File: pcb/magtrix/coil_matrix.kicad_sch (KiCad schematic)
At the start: 200 parts

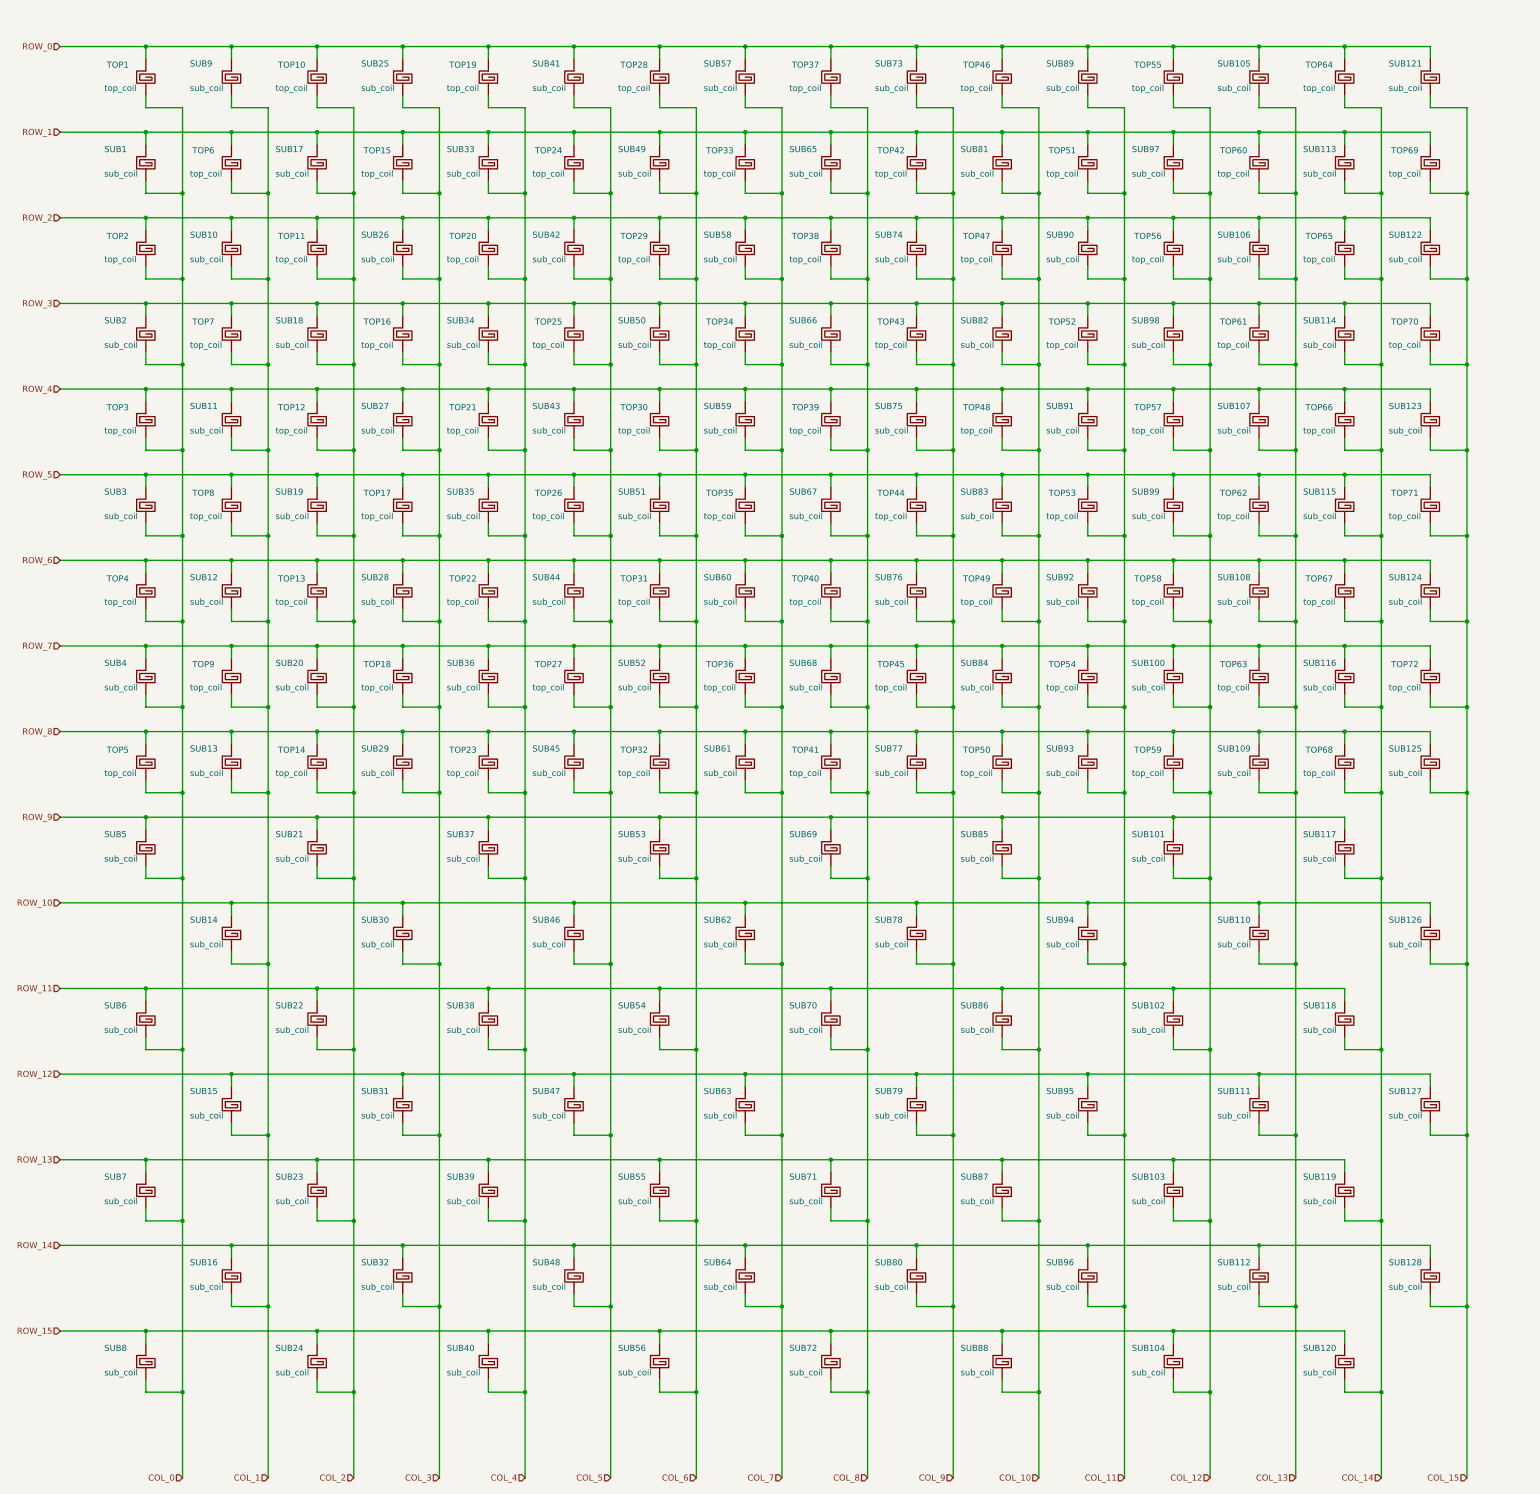
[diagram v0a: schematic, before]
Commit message: Finished schematics and footprints, need to redo the placement
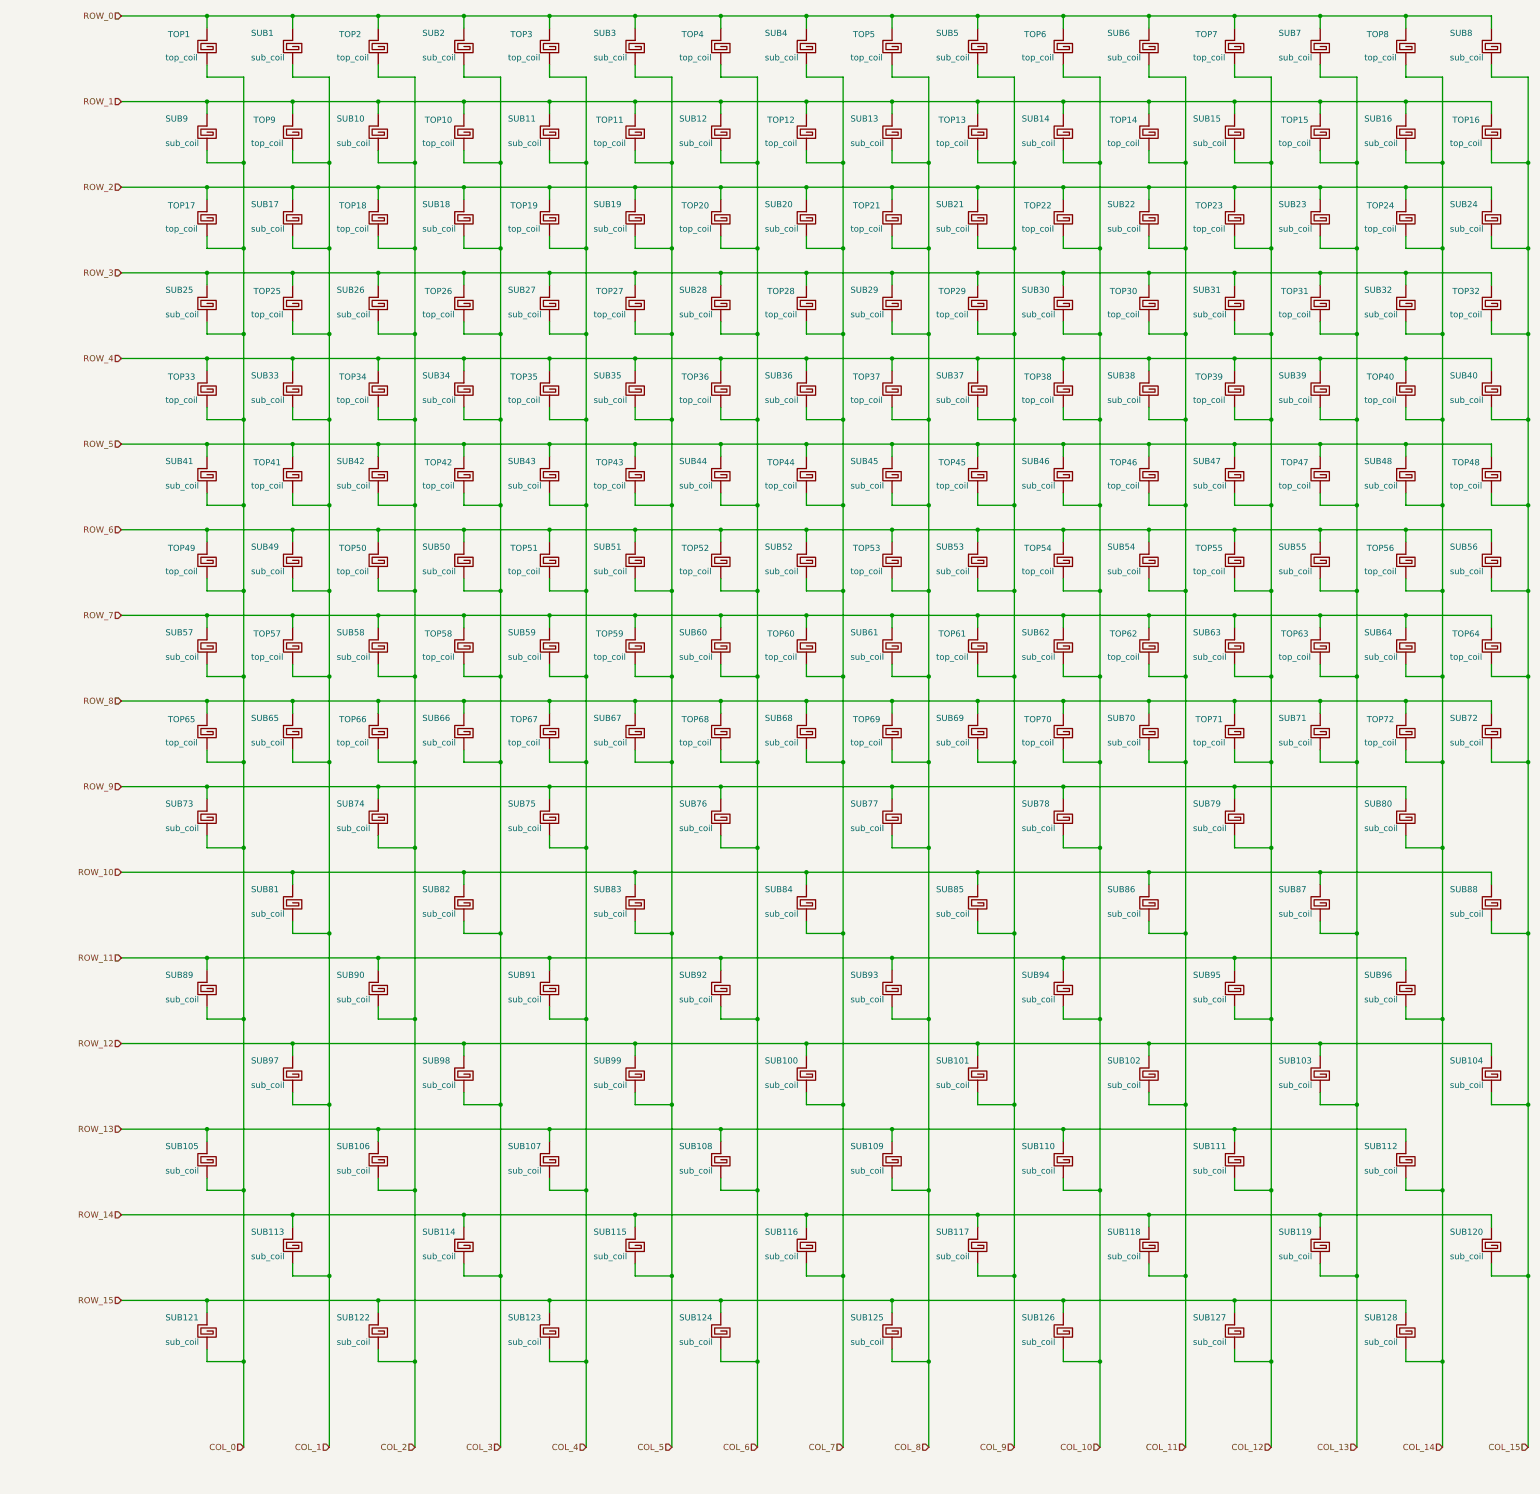
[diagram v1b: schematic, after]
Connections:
- net COL_0: now also SUB105.2 (B), SUB121.2 (B), SUB25.2 (B), SUB41.2 (B), SUB57.2 (B), SUB73.2 (B), SUB89.2 (B), SUB9.2 (B), TOP17.2 (B), TOP33.2 (B), TOP49.2 (B), TOP65.2 (B); no longer SUB1.2 (B), SUB2.2 (B), SUB3.2 (B), SUB4.2 (B), SUB5.2 (B), SUB6.2 (B), SUB7.2 (B), SUB8.2 (B), TOP2.2 (B), TOP3.2 (B), TOP4.2 (B), TOP5.2 (B)
- net COL_1: now also SUB1.2 (B), SUB113.2 (B), SUB17.2 (B), SUB33.2 (B), SUB49.2 (B), SUB65.2 (B), SUB81.2 (B), SUB97.2 (B), TOP25.2 (B), TOP41.2 (B), TOP57.2 (B); no longer SUB10.2 (B), SUB11.2 (B), SUB12.2 (B), SUB13.2 (B), SUB14.2 (B), SUB15.2 (B), SUB16.2 (B), SUB9.2 (B), TOP6.2 (B), TOP7.2 (B), TOP8.2 (B)
- net COL_10: now also SUB110.2 (B), SUB126.2 (B), SUB14.2 (B), SUB30.2 (B), SUB46.2 (B), SUB62.2 (B), SUB78.2 (B), SUB94.2 (B), TOP22.2 (B), TOP38.2 (B), TOP54.2 (B), TOP6.2 (B), TOP70.2 (B); no longer SUB81.2 (B), SUB82.2 (B), SUB83.2 (B), SUB84.2 (B), SUB85.2 (B), SUB86.2 (B), SUB87.2 (B), SUB88.2 (B), TOP46.2 (B), TOP47.2 (B), TOP48.2 (B), TOP49.2 (B), TOP50.2 (B)
- net COL_11: now also SUB102.2 (B), SUB118.2 (B), SUB22.2 (B), SUB38.2 (B), SUB54.2 (B), SUB6.2 (B), SUB70.2 (B), SUB86.2 (B), TOP14.2 (B), TOP30.2 (B), TOP46.2 (B), TOP62.2 (B); no longer SUB89.2 (B), SUB90.2 (B), SUB91.2 (B), SUB92.2 (B), SUB93.2 (B), SUB94.2 (B), SUB95.2 (B), SUB96.2 (B), TOP51.2 (B), TOP52.2 (B), TOP53.2 (B), TOP54.2 (B)
- net COL_12: now also SUB111.2 (B), SUB127.2 (B), SUB15.2 (B), SUB31.2 (B), SUB47.2 (B), SUB63.2 (B), SUB79.2 (B), SUB95.2 (B), TOP23.2 (B), TOP39.2 (B), TOP7.2 (B), TOP71.2 (B); no longer SUB100.2 (B), SUB101.2 (B), SUB102.2 (B), SUB103.2 (B), SUB104.2 (B), SUB97.2 (B), SUB98.2 (B), SUB99.2 (B), TOP56.2 (B), TOP57.2 (B), TOP58.2 (B), TOP59.2 (B)
- net COL_13: now also SUB103.2 (B), SUB119.2 (B), SUB23.2 (B), SUB39.2 (B), SUB55.2 (B), SUB7.2 (B), SUB71.2 (B), SUB87.2 (B), TOP15.2 (B), TOP31.2 (B), TOP47.2 (B); no longer SUB105.2 (B), SUB106.2 (B), SUB107.2 (B), SUB108.2 (B), SUB109.2 (B), SUB110.2 (B), SUB111.2 (B), SUB112.2 (B), TOP60.2 (B), TOP61.2 (B), TOP62.2 (B)
- net COL_14: now also SUB112.2 (B), SUB128.2 (B), SUB16.2 (B), SUB32.2 (B), SUB48.2 (B), SUB64.2 (B), SUB80.2 (B), SUB96.2 (B), TOP24.2 (B), TOP40.2 (B), TOP56.2 (B), TOP72.2 (B), TOP8.2 (B); no longer SUB113.2 (B), SUB114.2 (B), SUB115.2 (B), SUB116.2 (B), SUB117.2 (B), SUB118.2 (B), SUB119.2 (B), SUB120.2 (B), TOP64.2 (B), TOP65.2 (B), TOP66.2 (B), TOP67.2 (B), TOP68.2 (B)
- net COL_15: now also SUB104.2 (B), SUB120.2 (B), SUB24.2 (B), SUB40.2 (B), SUB56.2 (B), SUB72.2 (B), SUB8.2 (B), SUB88.2 (B), TOP16.2 (B), TOP32.2 (B), TOP48.2 (B), TOP64.2 (B); no longer SUB121.2 (B), SUB122.2 (B), SUB123.2 (B), SUB124.2 (B), SUB125.2 (B), SUB126.2 (B), SUB127.2 (B), SUB128.2 (B), TOP69.2 (B), TOP70.2 (B), TOP71.2 (B), TOP72.2 (B)
- net COL_2: now also SUB10.2 (B), SUB106.2 (B), SUB122.2 (B), SUB26.2 (B), SUB42.2 (B), SUB58.2 (B), SUB74.2 (B), SUB90.2 (B), TOP18.2 (B), TOP2.2 (B), TOP34.2 (B), TOP50.2 (B), TOP66.2 (B); no longer SUB17.2 (B), SUB18.2 (B), SUB19.2 (B), SUB20.2 (B), SUB21.2 (B), SUB22.2 (B), SUB23.2 (B), SUB24.2 (B), TOP10.2 (B), TOP11.2 (B), TOP12.2 (B), TOP13.2 (B), TOP14.2 (B)
- net COL_3: now also SUB114.2 (B), SUB18.2 (B), SUB2.2 (B), SUB34.2 (B), SUB50.2 (B), SUB66.2 (B), SUB82.2 (B), SUB98.2 (B), TOP10.2 (B), TOP26.2 (B), TOP42.2 (B), TOP58.2 (B); no longer SUB25.2 (B), SUB26.2 (B), SUB27.2 (B), SUB28.2 (B), SUB29.2 (B), SUB30.2 (B), SUB31.2 (B), SUB32.2 (B), TOP15.2 (B), TOP16.2 (B), TOP17.2 (B), TOP18.2 (B)
- net COL_4: now also SUB107.2 (B), SUB11.2 (B), SUB123.2 (B), SUB27.2 (B), SUB43.2 (B), SUB59.2 (B), SUB75.2 (B), SUB91.2 (B), TOP3.2 (B), TOP35.2 (B), TOP51.2 (B), TOP67.2 (B); no longer SUB33.2 (B), SUB34.2 (B), SUB35.2 (B), SUB36.2 (B), SUB37.2 (B), SUB38.2 (B), SUB39.2 (B), SUB40.2 (B), TOP20.2 (B), TOP21.2 (B), TOP22.2 (B), TOP23.2 (B)
- net COL_5: now also SUB115.2 (B), SUB19.2 (B), SUB3.2 (B), SUB35.2 (B), SUB51.2 (B), SUB67.2 (B), SUB83.2 (B), SUB99.2 (B), TOP11.2 (B), TOP43.2 (B), TOP59.2 (B); no longer SUB41.2 (B), SUB42.2 (B), SUB43.2 (B), SUB44.2 (B), SUB45.2 (B), SUB46.2 (B), SUB47.2 (B), SUB48.2 (B), TOP24.2 (B), TOP25.2 (B), TOP26.2 (B)
- net COL_6: now also SUB108.2 (B), SUB12.2 (B), SUB124.2 (B), SUB28.2 (B), SUB44.2 (B), SUB60.2 (B), SUB76.2 (B), SUB92.2 (B), TOP20.2 (B), TOP36.2 (B), TOP4.2 (B), TOP52.2 (B), TOP68.2 (B); no longer SUB49.2 (B), SUB50.2 (B), SUB51.2 (B), SUB52.2 (B), SUB53.2 (B), SUB54.2 (B), SUB55.2 (B), SUB56.2 (B), TOP28.2 (B), TOP29.2 (B), TOP30.2 (B), TOP31.2 (B), TOP32.2 (B)
- net COL_7: now also SUB100.2 (B), SUB116.2 (B), SUB20.2 (B), SUB36.2 (B), SUB4.2 (B), SUB52.2 (B), SUB68.2 (B), SUB84.2 (B), TOP12.2 (B), TOP28.2 (B), TOP44.2 (B), TOP60.2 (B); no longer SUB57.2 (B), SUB58.2 (B), SUB59.2 (B), SUB60.2 (B), SUB61.2 (B), SUB62.2 (B), SUB63.2 (B), SUB64.2 (B), TOP33.2 (B), TOP34.2 (B), TOP35.2 (B), TOP36.2 (B)
- net COL_8: now also SUB109.2 (B), SUB125.2 (B), SUB13.2 (B), SUB29.2 (B), SUB45.2 (B), SUB61.2 (B), SUB77.2 (B), SUB93.2 (B), TOP21.2 (B), TOP5.2 (B), TOP53.2 (B), TOP69.2 (B); no longer SUB65.2 (B), SUB66.2 (B), SUB67.2 (B), SUB68.2 (B), SUB69.2 (B), SUB70.2 (B), SUB71.2 (B), SUB72.2 (B), TOP38.2 (B), TOP39.2 (B), TOP40.2 (B), TOP41.2 (B)
- net COL_9: now also SUB101.2 (B), SUB117.2 (B), SUB21.2 (B), SUB37.2 (B), SUB5.2 (B), SUB53.2 (B), SUB69.2 (B), SUB85.2 (B), TOP13.2 (B), TOP29.2 (B), TOP61.2 (B); no longer SUB73.2 (B), SUB74.2 (B), SUB75.2 (B), SUB76.2 (B), SUB77.2 (B), SUB78.2 (B), SUB79.2 (B), SUB80.2 (B), TOP42.2 (B), TOP43.2 (B), TOP44.2 (B)
- net ROW_0: now also SUB1.1 (A), SUB2.1 (A), SUB3.1 (A), SUB4.1 (A), SUB5.1 (A), SUB6.1 (A), SUB7.1 (A), SUB8.1 (A), TOP2.1 (A), TOP3.1 (A), TOP4.1 (A), TOP5.1 (A), TOP6.1 (A), TOP7.1 (A), TOP8.1 (A); no longer SUB105.1 (A), SUB121.1 (A), SUB25.1 (A), SUB41.1 (A), SUB57.1 (A), SUB73.1 (A), SUB89.1 (A), SUB9.1 (A), TOP10.1 (A), TOP19.1 (A), TOP28.1 (A), TOP37.1 (A), TOP46.1 (A), TOP55.1 (A), TOP64.1 (A)
- net ROW_1: now also SUB10.1 (A), SUB11.1 (A), SUB12.1 (A), SUB13.1 (A), SUB14.1 (A), SUB15.1 (A), SUB16.1 (A), SUB9.1 (A), TOP10.1 (A), TOP11.1 (A), TOP12.1 (A), TOP13.1 (A), TOP14.1 (A), TOP16.1 (A), TOP9.1 (A); no longer SUB1.1 (A), SUB113.1 (A), SUB17.1 (A), SUB33.1 (A), SUB49.1 (A), SUB65.1 (A), SUB81.1 (A), SUB97.1 (A), TOP24.1 (A), TOP33.1 (A), TOP42.1 (A), TOP51.1 (A), TOP6.1 (A), TOP60.1 (A), TOP69.1 (A)
- net ROW_10: now also SUB81.1 (A), SUB82.1 (A), SUB83.1 (A), SUB84.1 (A), SUB85.1 (A), SUB86.1 (A), SUB87.1 (A), SUB88.1 (A); no longer SUB110.1 (A), SUB126.1 (A), SUB14.1 (A), SUB30.1 (A), SUB46.1 (A), SUB62.1 (A), SUB78.1 (A), SUB94.1 (A)
- net ROW_11: now also SUB89.1 (A), SUB90.1 (A), SUB91.1 (A), SUB92.1 (A), SUB93.1 (A), SUB94.1 (A), SUB95.1 (A), SUB96.1 (A); no longer SUB102.1 (A), SUB118.1 (A), SUB22.1 (A), SUB38.1 (A), SUB54.1 (A), SUB6.1 (A), SUB70.1 (A), SUB86.1 (A)
- net ROW_12: now also SUB100.1 (A), SUB101.1 (A), SUB102.1 (A), SUB103.1 (A), SUB104.1 (A), SUB97.1 (A), SUB98.1 (A), SUB99.1 (A); no longer SUB111.1 (A), SUB127.1 (A), SUB15.1 (A), SUB31.1 (A), SUB47.1 (A), SUB63.1 (A), SUB79.1 (A), SUB95.1 (A)
- net ROW_13: now also SUB105.1 (A), SUB106.1 (A), SUB107.1 (A), SUB108.1 (A), SUB109.1 (A), SUB110.1 (A), SUB111.1 (A), SUB112.1 (A); no longer SUB103.1 (A), SUB119.1 (A), SUB23.1 (A), SUB39.1 (A), SUB55.1 (A), SUB7.1 (A), SUB71.1 (A), SUB87.1 (A)
- net ROW_14: now also SUB113.1 (A), SUB114.1 (A), SUB115.1 (A), SUB116.1 (A), SUB117.1 (A), SUB118.1 (A), SUB119.1 (A), SUB120.1 (A); no longer SUB112.1 (A), SUB128.1 (A), SUB16.1 (A), SUB32.1 (A), SUB48.1 (A), SUB64.1 (A), SUB80.1 (A), SUB96.1 (A)
- net ROW_15: now also SUB121.1 (A), SUB122.1 (A), SUB123.1 (A), SUB124.1 (A), SUB125.1 (A), SUB126.1 (A), SUB127.1 (A), SUB128.1 (A); no longer SUB104.1 (A), SUB120.1 (A), SUB24.1 (A), SUB40.1 (A), SUB56.1 (A), SUB72.1 (A), SUB8.1 (A), SUB88.1 (A)
- net ROW_2: now also SUB17.1 (A), SUB18.1 (A), SUB19.1 (A), SUB20.1 (A), SUB21.1 (A), SUB22.1 (A), SUB23.1 (A), SUB24.1 (A), TOP17.1 (A), TOP18.1 (A), TOP19.1 (A), TOP21.1 (A), TOP22.1 (A), TOP23.1 (A), TOP24.1 (A); no longer SUB10.1 (A), SUB106.1 (A), SUB122.1 (A), SUB26.1 (A), SUB42.1 (A), SUB58.1 (A), SUB74.1 (A), SUB90.1 (A), TOP11.1 (A), TOP2.1 (A), TOP29.1 (A), TOP38.1 (A), TOP47.1 (A), TOP56.1 (A), TOP65.1 (A)
- net ROW_3: now also SUB25.1 (A), SUB26.1 (A), SUB27.1 (A), SUB28.1 (A), SUB29.1 (A), SUB30.1 (A), SUB31.1 (A), SUB32.1 (A), TOP26.1 (A), TOP27.1 (A), TOP28.1 (A), TOP29.1 (A), TOP30.1 (A), TOP31.1 (A), TOP32.1 (A); no longer SUB114.1 (A), SUB18.1 (A), SUB2.1 (A), SUB34.1 (A), SUB50.1 (A), SUB66.1 (A), SUB82.1 (A), SUB98.1 (A), TOP16.1 (A), TOP34.1 (A), TOP43.1 (A), TOP52.1 (A), TOP61.1 (A), TOP7.1 (A), TOP70.1 (A)
- net ROW_4: now also SUB33.1 (A), SUB34.1 (A), SUB35.1 (A), SUB36.1 (A), SUB37.1 (A), SUB38.1 (A), SUB39.1 (A), SUB40.1 (A), TOP33.1 (A), TOP34.1 (A), TOP35.1 (A), TOP36.1 (A), TOP37.1 (A), TOP38.1 (A), TOP40.1 (A); no longer SUB107.1 (A), SUB11.1 (A), SUB123.1 (A), SUB27.1 (A), SUB43.1 (A), SUB59.1 (A), SUB75.1 (A), SUB91.1 (A), TOP12.1 (A), TOP21.1 (A), TOP3.1 (A), TOP30.1 (A), TOP48.1 (A), TOP57.1 (A), TOP66.1 (A)
- net ROW_5: now also SUB41.1 (A), SUB42.1 (A), SUB43.1 (A), SUB44.1 (A), SUB45.1 (A), SUB46.1 (A), SUB47.1 (A), SUB48.1 (A), TOP41.1 (A), TOP42.1 (A), TOP43.1 (A), TOP45.1 (A), TOP46.1 (A), TOP47.1 (A), TOP48.1 (A); no longer SUB115.1 (A), SUB19.1 (A), SUB3.1 (A), SUB35.1 (A), SUB51.1 (A), SUB67.1 (A), SUB83.1 (A), SUB99.1 (A), TOP17.1 (A), TOP26.1 (A), TOP35.1 (A), TOP53.1 (A), TOP62.1 (A), TOP71.1 (A), TOP8.1 (A)
- net ROW_6: now also SUB49.1 (A), SUB50.1 (A), SUB51.1 (A), SUB52.1 (A), SUB53.1 (A), SUB54.1 (A), SUB55.1 (A), SUB56.1 (A), TOP50.1 (A), TOP51.1 (A), TOP52.1 (A), TOP53.1 (A), TOP54.1 (A), TOP55.1 (A), TOP56.1 (A); no longer SUB108.1 (A), SUB12.1 (A), SUB124.1 (A), SUB28.1 (A), SUB44.1 (A), SUB60.1 (A), SUB76.1 (A), SUB92.1 (A), TOP13.1 (A), TOP22.1 (A), TOP31.1 (A), TOP4.1 (A), TOP40.1 (A), TOP58.1 (A), TOP67.1 (A)
- net ROW_7: now also SUB57.1 (A), SUB58.1 (A), SUB59.1 (A), SUB60.1 (A), SUB61.1 (A), SUB62.1 (A), SUB63.1 (A), SUB64.1 (A), TOP57.1 (A), TOP58.1 (A), TOP59.1 (A), TOP60.1 (A), TOP61.1 (A), TOP62.1 (A), TOP64.1 (A); no longer SUB100.1 (A), SUB116.1 (A), SUB20.1 (A), SUB36.1 (A), SUB4.1 (A), SUB52.1 (A), SUB68.1 (A), SUB84.1 (A), TOP18.1 (A), TOP27.1 (A), TOP36.1 (A), TOP45.1 (A), TOP54.1 (A), TOP72.1 (A), TOP9.1 (A)
- net ROW_8: now also SUB65.1 (A), SUB66.1 (A), SUB67.1 (A), SUB68.1 (A), SUB69.1 (A), SUB70.1 (A), SUB71.1 (A), SUB72.1 (A), TOP65.1 (A), TOP66.1 (A), TOP67.1 (A), TOP69.1 (A), TOP70.1 (A), TOP71.1 (A), TOP72.1 (A); no longer SUB109.1 (A), SUB125.1 (A), SUB13.1 (A), SUB29.1 (A), SUB45.1 (A), SUB61.1 (A), SUB77.1 (A), SUB93.1 (A), TOP14.1 (A), TOP23.1 (A), TOP32.1 (A), TOP41.1 (A), TOP5.1 (A), TOP50.1 (A), TOP59.1 (A)
- net ROW_9: now also SUB73.1 (A), SUB74.1 (A), SUB75.1 (A), SUB76.1 (A), SUB77.1 (A), SUB78.1 (A), SUB79.1 (A), SUB80.1 (A); no longer SUB101.1 (A), SUB117.1 (A), SUB21.1 (A), SUB37.1 (A), SUB5.1 (A), SUB53.1 (A), SUB69.1 (A), SUB85.1 (A)

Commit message: Added finished PCB
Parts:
- removed SUB103, SUB104, SUB105, SUB106, SUB107, SUB108, SUB109, SUB110, SUB111, SUB112, SUB113, SUB114, SUB115, SUB116, SUB117, SUB118, SUB119, SUB120, SUB121, SUB122, SUB123, SUB124, SUB125, SUB126, SUB127, SUB128, SUB16, SUB23, SUB24, SUB32, SUB39, SUB40, SUB48, SUB55, SUB56, SUB64, SUB7, SUB71, SUB72, SUB8, SUB80, SUB87, SUB88, SUB96: sub_coil, libs:sub_coil, symbol square_coils:sub_coil
- removed TOP16, TOP24, TOP32, TOP40, TOP48, TOP56, TOP57, TOP58, TOP59, TOP60, TOP61, TOP62, TOP63, TOP64, TOP65, TOP66, TOP67, TOP68, TOP69, TOP70, TOP71, TOP72, TOP8: top_coil, libs:top_coil, symbol square_coils:top_coil
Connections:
- net COL_13 is gone; now on net COL_12: TOP15.2 (B), TOP31.2 (B), TOP47.2 (B)
- net COL_0: now also TOP25.2 (B), TOP41.2 (B), TOP9.2 (B)
- net COL_1: no longer TOP25.2 (B), TOP41.2 (B), TOP9.2 (B)
- net COL_10: now also TOP14.2 (B), TOP30.2 (B), TOP46.2 (B)
- net COL_11: no longer TOP14.2 (B), TOP30.2 (B), TOP46.2 (B)
- net COL_2: now also TOP10.2 (B), TOP26.2 (B), TOP42.2 (B)
- net COL_3: no longer TOP10.2 (B), TOP26.2 (B), TOP42.2 (B)
- net COL_4: now also TOP11.2 (B), TOP27.2 (B), TOP43.2 (B)
- net COL_5: no longer TOP11.2 (B), TOP27.2 (B), TOP43.2 (B)
- net COL_6: now also TOP12.2 (B), TOP28.2 (B), TOP44.2 (B)
- net COL_7: no longer TOP12.2 (B), TOP28.2 (B), TOP44.2 (B)
- net COL_8: now also TOP13.2 (B), TOP29.2 (B), TOP45.2 (B)
- net COL_9: no longer TOP13.2 (B), TOP29.2 (B), TOP45.2 (B)
- net ROW_1: now also SUB17.1 (A), SUB18.1 (A), SUB19.1 (A), SUB20.1 (A), SUB21.1 (A), SUB22.1 (A); no longer TOP10.1 (A), TOP11.1 (A), TOP12.1 (A), TOP13.1 (A), TOP14.1 (A), TOP15.1 (A), TOP9.1 (A)
- net ROW_10: now also TOP41.1 (A), TOP42.1 (A), TOP43.1 (A), TOP44.1 (A), TOP45.1 (A), TOP46.1 (A), TOP47.1 (A); no longer SUB81.1 (A), SUB82.1 (A), SUB83.1 (A), SUB84.1 (A), SUB85.1 (A), SUB86.1 (A)
- net ROW_12: now also TOP49.1 (A), TOP50.1 (A), TOP51.1 (A), TOP52.1 (A), TOP53.1 (A), TOP54.1 (A), TOP55.1 (A); no longer SUB100.1 (A), SUB101.1 (A), SUB102.1 (A), SUB97.1 (A), SUB98.1 (A), SUB99.1 (A)
- net ROW_2: now also SUB33.1 (A), SUB34.1 (A), SUB35.1 (A), SUB36.1 (A), SUB37.1 (A), SUB38.1 (A), TOP10.1 (A), TOP11.1 (A), TOP12.1 (A), TOP13.1 (A), TOP14.1 (A), TOP15.1 (A), TOP9.1 (A); no longer SUB17.1 (A), SUB18.1 (A), SUB19.1 (A), SUB20.1 (A), SUB21.1 (A), SUB22.1 (A), TOP17.1 (A), TOP18.1 (A), TOP19.1 (A), TOP20.1 (A), TOP21.1 (A), TOP22.1 (A), TOP23.1 (A)
- net ROW_3: now also SUB49.1 (A), SUB50.1 (A), SUB51.1 (A), SUB52.1 (A), SUB53.1 (A), SUB54.1 (A); no longer TOP25.1 (A), TOP26.1 (A), TOP27.1 (A), TOP28.1 (A), TOP29.1 (A), TOP30.1 (A), TOP31.1 (A)
- net ROW_4: now also SUB65.1 (A), SUB66.1 (A), SUB67.1 (A), SUB68.1 (A), SUB69.1 (A), SUB70.1 (A), TOP17.1 (A), TOP18.1 (A), TOP19.1 (A), TOP20.1 (A), TOP21.1 (A), TOP22.1 (A), TOP23.1 (A); no longer SUB33.1 (A), SUB34.1 (A), SUB35.1 (A), SUB36.1 (A), SUB37.1 (A), SUB38.1 (A), TOP33.1 (A), TOP34.1 (A), TOP35.1 (A), TOP36.1 (A), TOP37.1 (A), TOP38.1 (A), TOP39.1 (A)
- net ROW_5: now also SUB81.1 (A), SUB82.1 (A), SUB83.1 (A), SUB84.1 (A), SUB85.1 (A), SUB86.1 (A); no longer TOP41.1 (A), TOP42.1 (A), TOP43.1 (A), TOP44.1 (A), TOP45.1 (A), TOP46.1 (A), TOP47.1 (A)
- net ROW_6: now also SUB100.1 (A), SUB101.1 (A), SUB102.1 (A), SUB97.1 (A), SUB98.1 (A), SUB99.1 (A), TOP25.1 (A), TOP26.1 (A), TOP27.1 (A), TOP28.1 (A), TOP29.1 (A), TOP30.1 (A), TOP31.1 (A); no longer SUB49.1 (A), SUB50.1 (A), SUB51.1 (A), SUB52.1 (A), SUB53.1 (A), SUB54.1 (A), TOP49.1 (A), TOP50.1 (A), TOP51.1 (A), TOP52.1 (A), TOP53.1 (A), TOP54.1 (A), TOP55.1 (A)
- net ROW_8: now also TOP33.1 (A), TOP34.1 (A), TOP35.1 (A), TOP36.1 (A), TOP37.1 (A), TOP38.1 (A), TOP39.1 (A); no longer SUB65.1 (A), SUB66.1 (A), SUB67.1 (A), SUB68.1 (A), SUB69.1 (A), SUB70.1 (A)
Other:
- moved on the sheet: SUB100, SUB101, SUB102, SUB17, SUB18, SUB19, SUB20, SUB21, SUB22, SUB33, SUB34, SUB35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
